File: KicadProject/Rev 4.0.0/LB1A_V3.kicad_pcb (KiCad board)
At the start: 6 copper layers, 42 x 42 mm, 187 parts, among them J601 2337019-1, J602 2337019-1, U101 STM32MP157CAA3, U201 AS4C256M16D3LC-12BCN, U401 STPMIC1xPQR, U501 S40FC004C1B2C00000, U601 LBEE59B1LV-278, U701 DF40C-70DP-0.4V(51), U702 DF40C-100DP-0.4V(51), U703 DF40C-100DP-0.4V(51), X101 32.768kHz, Y101 24MHz

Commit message: another trace
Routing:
- net /MPU_DDR3L_Memory/DDR_DQ4: track 0.00 -> 39.9 mm, vias 0 -> 2
- net /MPU_DDR3L_Memory/DDR_RESETN: track 0.00 -> 0.42 mm, vias 0 -> 1
- net /MPU_DDR3L_Memory/DDR_A13: track 0.00 -> 0.42 mm, vias 0 -> 1
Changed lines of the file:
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@@
     (thickness 1.2)
     (drawings 8)
-    (tracks 1498)
+    (tracks 1564)
     (zones 0)
     (modules 187)
@@
   (segment (start 197.24 106.16) (end 197.24 105.35) (width 0.127) (layer L1_Sig_Pwr.Cu) (net 46))
   (segment (start 196.7 106.7) (end 197.24 106.16) (width 0.127) (layer L1_Sig_Pwr.Cu) (net 46))
+  (via (at 196.9 102.5) (size 0.4) (drill 0.2) (layers L1_Sig_Pwr.Cu L6_Sig_Pwr.Cu) (net 52))
+  (segment (start 197.2 102.2) (end 196.9 102.5) (width 0.127) (layer L1_Sig_Pwr.Cu) (net 52))
+  (via (at 196.1 102.5) (size 0.4) (drill 0.2) (layers L1_Sig_Pwr.Cu L6_Sig_Pwr.Cu) (net 57))
+  (segment (start 196.4 102.2) (end 196.1 102.5) (width 0.127) (layer L1_Sig_Pwr.Cu) (net 57))
   (via (at 184.19 100.5) (size 0.4) (drill 0.2) (layers L1_Sig_Pwr.Cu L6_Sig_Pwr.Cu) (net 67))
   (segment (start 184.15 100.46) (end 184.19 100.5) (width 0.2) (layer L1_Sig_Pwr.Cu) (net 67))
@@
   (segment (start 189.18351 88.59149) (end 189.45 88.325) (width 0.127) (layer L1_Sig_Pwr.Cu) (net 154))
   (segment (start 189.18351 93.33351) (end 189.18351 88.59149) (width 0.127) (layer L1_Sig_Pwr.Cu) (net 154))
-  (via (at 201.6 89.7) (size 0.4) (drill 0.15) (layers L1_Sig_Pwr.Cu L6_Sig_Pwr.Cu) (net 154))
+  (via (at 201.6 89.7) (size 0.4) (drill 0.2) (layers L1_Sig_Pwr.Cu L6_Sig_Pwr.Cu) (net 154))
   (segment (start 200.768501 92.231499) (end 200.4 92.6) (width 0.127) (layer L1_Sig_Pwr.Cu) (net 154))
   (segment (start 201.313883 92.231499) (end 200.768501 92.231499) (width 0.127) (layer L1_Sig_Pwr.Cu) (net 154))
@@
   (segment (start 191.5 95.6) (end 194 95.6) (width 0.127) (layer L3_Sig_Pwr.Cu) (net 179))
   (via (at 194.3 93.6) (size 0.4) (drill 0.15) (layers L1_Sig_Pwr.Cu L6_Sig_Pwr.Cu) (net 180))
-  (via (at 198.7 90.3) (size 0.4) (drill 0.15) (layers L1_Sig_Pwr.Cu L6_Sig_Pwr.Cu) (net 180))
+  (via (at 198.7 90.3) (size 0.4) (drill 0.2) (layers L1_Sig_Pwr.Cu L6_Sig_Pwr.Cu) (net 180))
   (segment (start 197.3 90.3) (end 197.2 90.2) (width 0.127) (layer L1_Sig_Pwr.Cu) (net 180))
   (segment (start 198.7 90.3) (end 197.3 90.3) (width 0.127) (layer L1_Sig_Pwr.Cu) (net 180))
@@
   (segment (start 196.3 89.6) (end 196.4 89.7) (width 0.127) (layer L1_Sig_Pwr.Cu) (net 181))
   (segment (start 196.4 89.7) (end 196.4 90.2) (width 0.127) (layer L1_Sig_Pwr.Cu) (net 181))
+  (segment (start 196.5 104.6) (end 196.4 104.5) (width 0.127) (layer L1_Sig_Pwr.Cu) (net 188))
+  (segment (start 196.8 103) (end 196.8 104.2) (width 0.127) (layer L1_Sig_Pwr.Cu) (net 188))
+  (segment (start 197.6 100.4) (end 197.6 102.6) (width 0.127) (layer L1_Sig_Pwr.Cu) (net 188))
+  (segment (start 196.2 107.900001) (end 196.2 107.9) (width 0.127) (layer L1_Sig_Pwr.Cu) (net 188))
+  (segment (start 196.9 102.9) (end 196.8 103) (width 0.127) (layer L1_Sig_Pwr.Cu) (net 188))
+  (segment (start 197.3 104.3) (end 197.2 104.2) (width 0.127) (layer L1_Sig_Pwr.Cu) (net 188))
+  (segment (start 195.9 108.200001) (end 196.2 107.900001) (width 0.127) (layer L1_Sig_Pwr.Cu) (net 188))
+  (segment (start 197.5 104.3) (end 197.3 104.3) (width 0.127) (layer L1_Sig_Pwr.Cu) (net 188))
+  (segment (start 197.6 104.2) (end 197.5 104.3) (width 0.127) (layer L1_Sig_Pwr.Cu) (net 188))
+  (segment (start 197.6 102.6) (end 197.6 104.2) (width 0.127) (layer L1_Sig_Pwr.Cu) (net 188))
+  (segment (start 196.4 104.5) (end 196.4 103.1) (width 0.127) (layer L1_Sig_Pwr.Cu) (net 188))
+  (segment (start 197.2 104.2) (end 197.2 103) (width 0.127) (layer L1_Sig_Pwr.Cu) (net 188))
+  (segment (start 196.7 104.6) (end 196.5 104.6) (width 0.127) (layer L1_Sig_Pwr.Cu) (net 188))
+  (segment (start 196.3 107.8) (end 196.3 106.4) (width 0.127) (layer L1_Sig_Pwr.Cu) (net 188))
+  (segment (start 196 103) (end 196 104.1) (width 0.127) (layer L1_Sig_Pwr.Cu) (net 188))
+  (segment (start 197.1 104.7) (end 197.9 104.7) (width 0.127) (layer L1_Sig_Pwr.Cu) (net 188))
+  (segment (start 196.8 104.2) (end 196.8 104.5) (width 0.127) (layer L1_Sig_Pwr.Cu) (net 188))
+  (segment (start 196.8 105.9) (end 196.8 105) (width 0.127) (layer L1_Sig_Pwr.Cu) (net 188))
+  (segment (start 197.1 102.9) (end 196.9 102.9) (width 0.127) (layer L1_Sig_Pwr.Cu) (net 188))
+  (segment (start 196.2 107.9) (end 196.3 107.8) (width 0.127) (layer L1_Sig_Pwr.Cu) (net 188))
+  (segment (start 196.4 103.1) (end 196.4 103) (width 0.127) (layer L1_Sig_Pwr.Cu) (net 188))
+  (segment (start 196.8 105) (end 197.1 104.7) (width 0.127) (layer L1_Sig_Pwr.Cu) (net 188))
+  (segment (start 195.6 103.1) (end 195.5 103) (width 0.127) (layer L1_Sig_Pwr.Cu) (net 188))
+  (segment (start 197.7 100.3) (end 197.6 100.4) (width 0.127) (layer L1_Sig_Pwr.Cu) (net 188))
+  (segment (start 197.9 104.7) (end 198 104.6) (width 0.127) (layer L1_Sig_Pwr.Cu) (net 188))
+  (segment (start 196.8 104.5) (end 196.7 104.6) (width 0.127) (layer L1_Sig_Pwr.Cu) (net 188))
+  (segment (start 198 104.6) (end 198 100.4) (width 0.127) (layer L1_Sig_Pwr.Cu) (net 188))
+  (segment (start 197.2 103) (end 197.1 102.9) (width 0.127) (layer L1_Sig_Pwr.Cu) (net 188))
+  (segment (start 197.9 100.3) (end 197.7 100.3) (width 0.127) (layer L1_Sig_Pwr.Cu) (net 188))
+  (segment (start 196.3 106.4) (end 196.8 105.9) (width 0.127) (layer L1_Sig_Pwr.Cu) (net 188))
+  (segment (start 198 100.4) (end 197.9 100.3) (width 0.127) (layer L1_Sig_Pwr.Cu) (net 188))
+  (segment (start 196.4 103) (end 196.3 102.9) (width 0.127) (layer L1_Sig_Pwr.Cu) (net 188))
+  (segment (start 196.3 102.9) (end 196.1 102.9) (width 0.127) (layer L1_Sig_Pwr.Cu) (net 188))
+  (segment (start 196.1 102.9) (end 196 103) (width 0.127) (layer L1_Sig_Pwr.Cu) (net 188))
+  (segment (start 196 104.1) (end 196 104.2) (width 0.127) (layer L1_Sig_Pwr.Cu) (net 188))
+  (segment (start 196 104.2) (end 195.9 104.3) (width 0.127) (layer L1_Sig_Pwr.Cu) (net 188))
+  (segment (start 195.9 104.3) (end 195.7 104.3) (width 0.127) (layer L1_Sig_Pwr.Cu) (net 188))
+  (segment (start 195.7 104.3) (end 195.6 104.2) (width 0.127) (layer L1_Sig_Pwr.Cu) (net 188))
+  (segment (start 195.6 104.2) (end 195.6 103.2) (width 0.127) (layer L1_Sig_Pwr.Cu) (net 188))
+  (segment (start 195.6 103.2) (end 195.6 103.1) (width 0.127) (layer L1_Sig_Pwr.Cu) (net 188))
+  (segment (start 195.5 103) (end 195 103) (width 0.127) (layer L1_Sig_Pwr.Cu) (net 188))
+  (segment (start 195 103) (end 194.9 103) (width 0.127) (layer L1_Sig_Pwr.Cu) (net 188))
+  (segment (start 194.9 103) (end 194.8 102.9) (width 0.127) (layer L1_Sig_Pwr.Cu) (net 188))
+  (segment (start 194.8 102.9) (end 194.8 101.3) (width 0.127) (layer L1_Sig_Pwr.Cu) (net 188))
+  (segment (start 194.8 101.3) (end 194.8 100.862018) (width 0.127) (layer L1_Sig_Pwr.Cu) (net 188))
+  (segment (start 194.8 100.862018) (end 195.231499 100.430519) (width 0.127) (layer L1_Sig_Pwr.Cu) (net 188))
+  (segment (start 195.231499 100.430519) (end 195.231499 98.631499) (width 0.127) (layer L1_Sig_Pwr.Cu) (net 188))
+  (segment (start 195.231499 98.631499) (end 194.8 98.2) (width 0.127) (layer L1_Sig_Pwr.Cu) (net 188))
+  (via (at 196.1 92.1) (size 0.4) (drill 0.15) (layers L1_Sig_Pwr.Cu L6_Sig_Pwr.Cu) (net 188))
+  (segment (start 196.4 91.8) (end 196.1 92.1) (width 0.127) (layer L1_Sig_Pwr.Cu) (net 188))
+  (via (at 194.8 97.5) (size 0.4) (drill 0.2) (layers L1_Sig_Pwr.Cu L6_Sig_Pwr.Cu) (net 188))
+  (segment (start 194.8 98.2) (end 194.8 97.5) (width 0.127) (layer L1_Sig_Pwr.Cu) (net 188))
+  (segment (start 195 92.4) (end 195.236499 92.163501) (width 0.127) (layer L3_Sig_Pwr.Cu) (net 188))
+  (segment (start 196.036499 92.163501) (end 196.1 92.1) (width 0.127) (layer L3_Sig_Pwr.Cu) (net 188))
+  (segment (start 195 97) (end 195 92.4) (width 0.127) (layer L3_Sig_Pwr.Cu) (net 188))
+  (segment (start 194.9 97.1) (end 195 97) (width 0.127) (layer L3_Sig_Pwr.Cu) (net 188))
+  (segment (start 192.7 97.4) (end 192.7 97.2) (width 0.127) (layer L3_Sig_Pwr.Cu) (net 188))
+  (segment (start 195.236499 92.163501) (end 196.036499 92.163501) (width 0.127) (layer L3_Sig_Pwr.Cu) (net 188))
+  (segment (start 192.7 97.2) (end 192.8 97.1) (width 0.127) (layer L3_Sig_Pwr.Cu) (net 188))
+  (segment (start 192.8 97.5) (end 192.7 97.4) (width 0.127) (layer L3_Sig_Pwr.Cu) (net 188))
+  (segment (start 192.8 97.1) (end 194.9 97.1) (width 0.127) (layer L3_Sig_Pwr.Cu) (net 188))
+  (segment (start 194.8 97.5) (end 192.8 97.5) (width 0.127) (layer L3_Sig_Pwr.Cu) (net 188))
   (segment (start 184.15 94.330698) (end 184.330698 94.15) (width 0.127) (layer L1_Sig_Pwr.Cu) (net 207))
   (segment (start 184.15 94.75) (end 184.15 94.330698) (width 0.127) (layer L1_Sig_Pwr.Cu) (net 207))

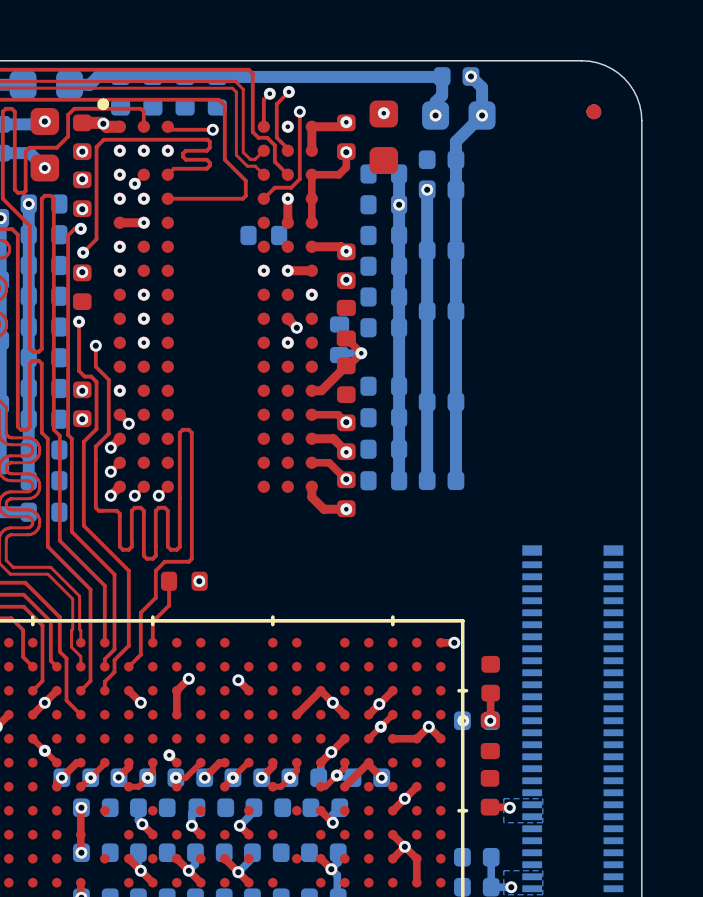
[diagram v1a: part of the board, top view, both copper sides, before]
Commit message: some more traces
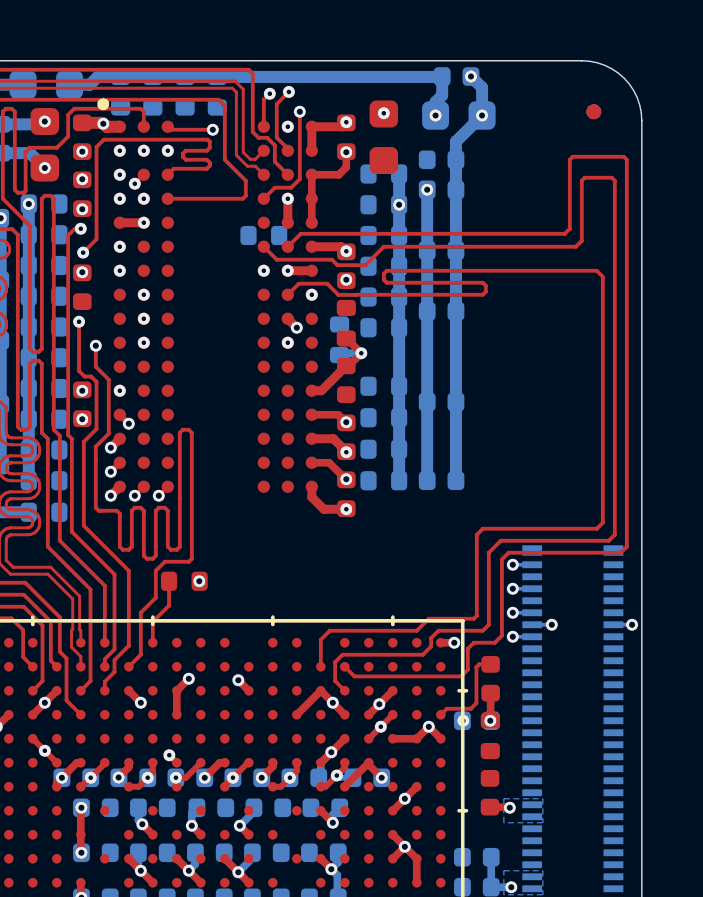
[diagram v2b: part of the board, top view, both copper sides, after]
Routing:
- net /MPU_DDR3L_Memory/DDR_DQ15: track 0.00 -> 40.1 mm
- net /MPU_DDR3L_Memory/DDR_DQ14: track 0.00 -> 40.0 mm
- net /MPU_DDR3L_Memory/DDR_DQ12: track 0.00 -> 39.9 mm
- net PMIC_VREF_DDR: track 1.63 -> 4.69 mm
- net PK5: track 0.00 -> 0.66 mm, vias 0 -> 1
- net PK7: track 0.00 -> 0.65 mm, vias 0 -> 1
- net PK3: track 0.00 -> 0.65 mm, vias 0 -> 1
- net DSI_D0_N: track 0.00 -> 0.65 mm, vias 0 -> 1
- net DSI_CK_N: track 0.00 -> 0.65 mm, vias 0 -> 1
- net PK4: track 0.00 -> 0.62 mm, vias 0 -> 1
